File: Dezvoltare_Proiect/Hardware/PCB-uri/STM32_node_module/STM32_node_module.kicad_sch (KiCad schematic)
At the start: 4 parts, among them U1 STM32F411RETx, U2 ATECC608B-SSHDA, U3 SHT30A-DIS

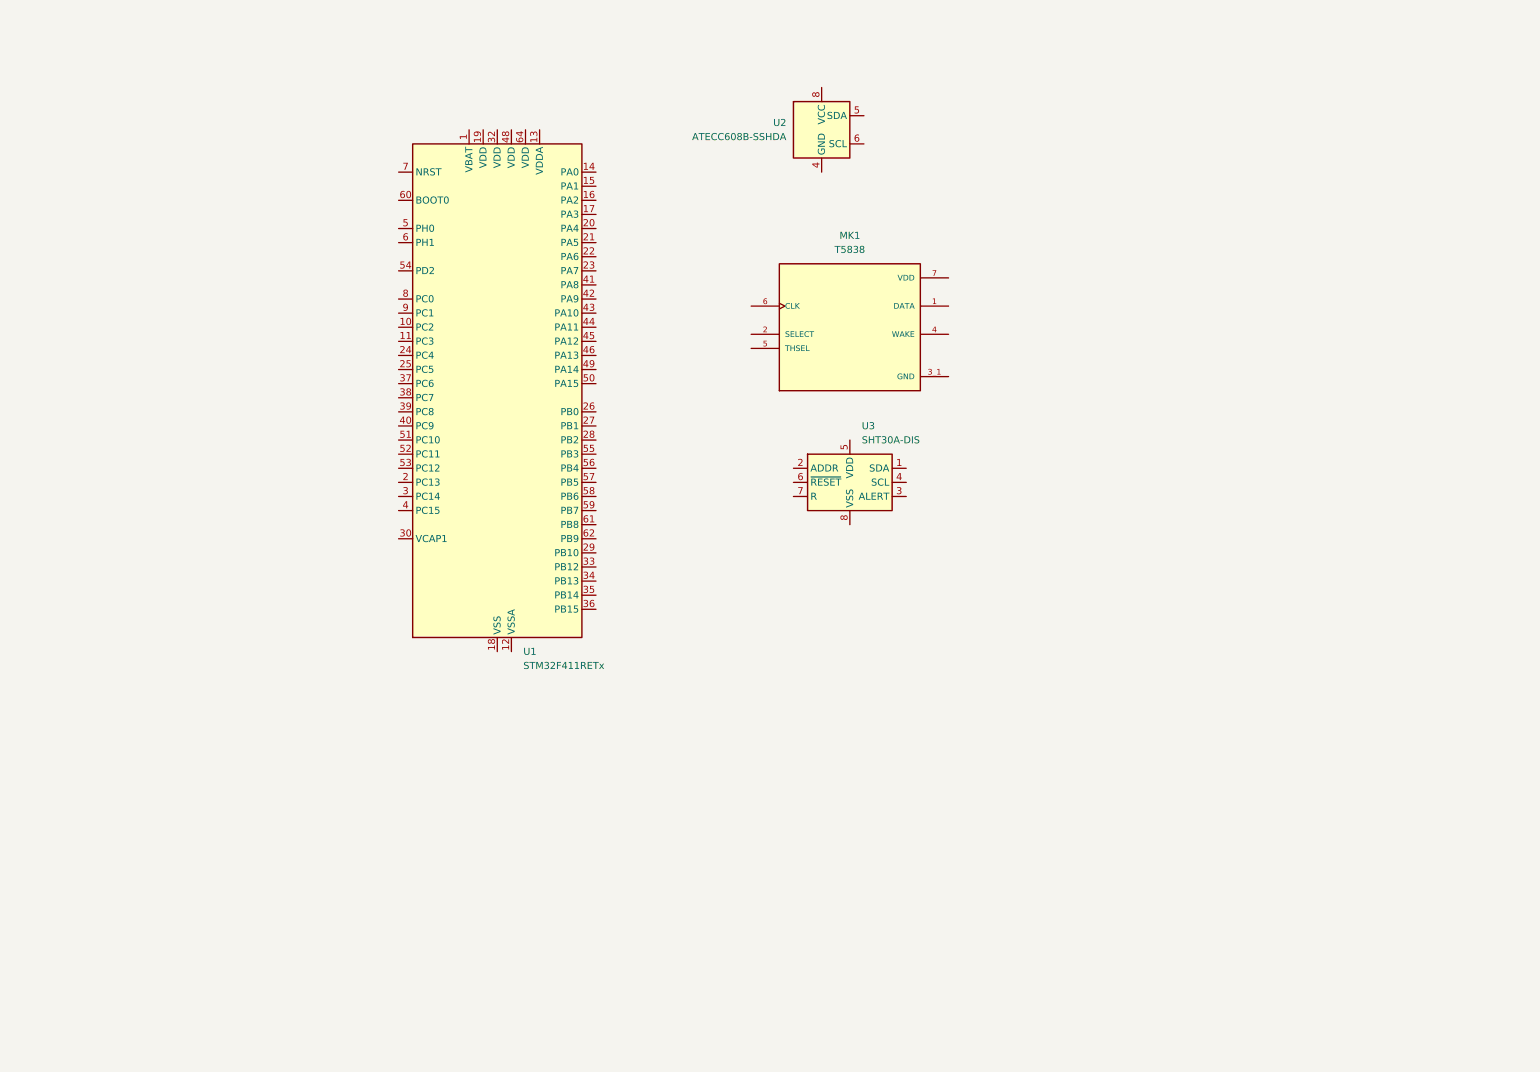
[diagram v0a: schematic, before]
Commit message: Actualizare PCB-uri, componente custom, acces la documentatia de pe overleaf.
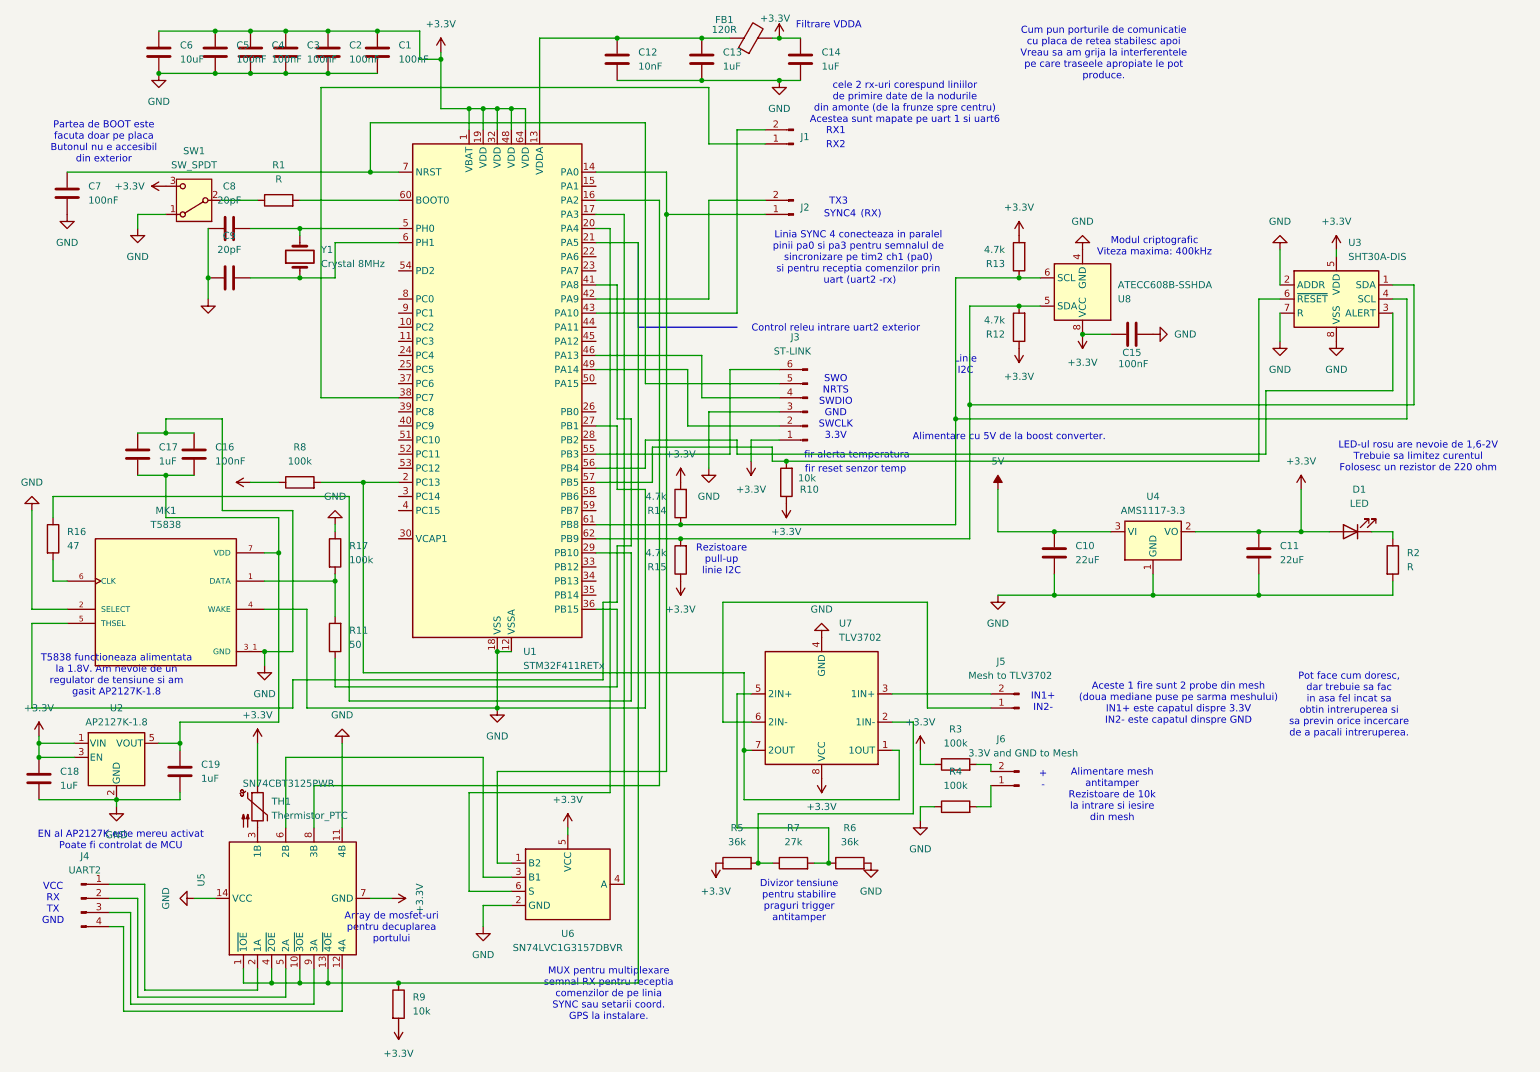
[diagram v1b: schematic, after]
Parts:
- removed U2: ATECC608B-SSHDA, Package_SO:SOIC-8_3.9x4.9mm_P1.27mm, symbol Security:ATECC608B-SSHDA
- added C1, C15, C16, C2, C3, C4, C5, C7: 100nF, symbol Device:C
- added C10, C11: 22uF, symbol Device:C
- added C12: 10nF, symbol Device:C
- added C13, C14, C17, C18, C19: 1uF, symbol Device:C
- added C6: 10uF, symbol Device:C
- added C8, C9: 20pF, symbol Device:C
- added D1: LED, symbol Device:LED
- added FB1: 120R, symbol Device:FerriteBead
- added J1, J2: (no value), symbol Connector:Conn_01x02_Pin
- added J3: ST-LINK, symbol Connector:Conn_01x06_Pin
- added J4: UART2, symbol Connector:Conn_01x04_Pin
- added J5: Mesh to TLV3702, symbol Connector:Conn_01x02_Pin
- added J6: 3.3V and GND to Mesh, symbol Connector:Conn_01x02_Pin
- added R1, R2: R, symbol Device:R
- added R10, R9: 10k, symbol Device:R
- added R11: 50, symbol Device:R
- added R12, R13, R14, R15: 4.7k, symbol Device:R
- added R16: 47, symbol Device:R
- added R17, R3, R4, R8: 100k, symbol Device:R
- added R5, R6: 36k, symbol Device:R
- added R7: 27k, symbol Device:R
- added SW1: SW_SPDT, symbol Switch:SW_SPDT
- added TH1: Thermistor_PTC, symbol Device:Thermistor_PTC
- added U2: AP2127K-1.8, Package_TO_SOT_SMD:SOT-23-5, symbol Regulator_Linear:AP2127K-1.8
- added U4: AMS1117-3.3, Package_TO_SOT_SMD:SOT-223-3_TabPin2, symbol Regulator_Linear:AMS1117-3.3
- added U5: SN74CBT3125PWR, Custom_Footprints:TSSOP-14_PW14_TI, symbol SN74CBT3125_PW:SN74CBT3125PWR
- added U6: SN74LVC1G3157DBVR, Custom_Footprints:SOT-23-6_DBV0006A, symbol SN74LVC1G3157_DBV:SN74LVC1G3157DBVR
- added U7: TLV3702, Custom_Footprints:SOIC-8_3.9x4.9mm_P1.27mm, symbol TLV3702:TLV3702
- added U8: ATECC608B-SSHDA, Package_SO:SOIC-8_3.9x4.9mm_P1.27mm, symbol Security:ATECC608B-SSHDA
- added Y1: Crystal 8MHz, symbol Device:Crystal
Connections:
- net GND: now also MK1.2 (SELECT), MK1.4 (WAKE), U1.12 (VSSA), U1.18 (VSS), U1.27 (PB1), U1.31 (VSS), U1.47 (VSS), U1.63 (VSS), U3.2 (ADDR), U3.7 (R), U3.8 (VSS), U3.9 (VSS), C1.2, C10.2, C11.2, C12.2, C13.2, C14.2, C15.2, C16.2, C17.1, C18.2, C19.2, C2.2, C3.2, C4.2, C5.2, C6.2, C7.2, C8.1, C9.1, J3.3 (Pin_3), R17.1, R2.2, R4.1, R6.2, SW1.1 (A), U2.2 (GND), U4.1 (GND), U5.11 (4B), U5.14 (VCC), U6.2 (GND), U7.4 (GND), U8.4 (GND)
- net +3.3V: now reaches U1.1 (VBAT)
- net +3.3V: now also U1.19 (VDD), U1.32 (VDD), U1.48 (VDD), U1.64 (VDD), U3.5 (VDD), C1.1, C11.1, C14.1, C15.1, C18.1, C2.1, C3.1, C4.1, C5.1, C6.1, D1.2 (A), FB1.2, J3.1 (Pin_1), R10.1, R12.1, R13.2, R14.2, R15.1, R3.1, R5.1, R8.1, R9.2, SW1.3 (C), TH1.1, U2.1 (VIN), U2.3 (EN), U4.2 (VO), U5.7 (GND), U6.5 (VCC), U7.8 (VCC), U8.8 (VCC)
- net at U1.13 (VDDA): now also C12.1, C13.1, FB1.1
- net at U1.14 (PA0): now also J2.1 (Pin_1), U6.1 (B2)
- net at U1.16 (PA2): now also U5.8 (3B)
- net at U1.17 (PA3): now also U6.4 (A)
- net at U1.2 (PC13): now also R8.2, U7.1 (1OUT), U7.7 (2OUT)
- net at U1.20 (PA4): now also U6.6 (S)
- net at U1.21 (PA5): now also R9.1, U5.1 (~{1OE}), U5.10 (~{3OE}), U5.13 (~{4OE}), U5.4 (~{2OE})
- net at U1.29 (PB10): now also R16.1
- net at U1.36 (PB15): now also R11.1
- net at U1.38 (PC7): now also J1.1 (Pin_1)
- net at U1.41 (PA8): now also MK1.5 (THSEL)
- net at U1.42 (PA9): now also J2.2 (Pin_2)
- net at U1.43 (PA10): now also J1.2 (Pin_2)
- net at U1.46 (PA13): now also J3.4 (Pin_4)
- net at U1.49 (PA14): now also J3.2 (Pin_2)
- net at U1.5 (PH0): now also C8.2, Y1.2
- net at U1.55 (PB3): now also J3.6 (Pin_6)
- net at U1.56 (PB4): now also U3.3 (ALERT)
- net at U1.57 (PB5): now also U3.6 (~{RESET}), R10.2
- net at U1.6 (PH1): now also C9.2, Y1.1
- net at U1.60 (BOOT0): now also R1.2
- net at U1.61 (PB8): now also U3.4 (SCL), R13.1, R14.1, U8.6 (SCL)
- net at U1.62 (PB9): now also U3.1 (SDA), R12.2, R15.2, U8.5 (SDA)
- net at U1.7 (NRST): now also C7.1, J3.5 (Pin_5)
- net at MK1.1 (DATA): now also R11.2, R17.2
- net at MK1.6 (CLK): now also R16.2
- net at MK1.7 (VDD): now also C16.1, C17.2, C19.1, U2.5 (VOUT)
- new net: J4.4 (Pin_4), U5.12 (4A)
- new net: J4.1 (Pin_1), U5.2 (1A)
- new net: TH1.2, U5.3 (1B)
- new net: J4.2 (Pin_2), U5.5 (2A)
- new net: U5.6 (2B), U6.3 (B1)
- new net: J4.3 (Pin_3), U5.9 (3A)
- new net: R5.2, R7.1, U7.2 (1IN-)
- new net: R6.1, R7.2, U7.5 (2IN+)
- new net: J6.1 (Pin_1), R4.2
- new net: J6.2 (Pin_2), R3.2
- new net: J5.1 (Pin_1), U7.6 (2IN-)
- new net: J5.2 (Pin_2), U7.3 (1IN+)
- new net: R1.1, SW1.2 (B)
- new net: D1.1 (K), R2.1
- new net 5V: C10.1, U4.3 (VI)
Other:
- note added: "(RX)"
- note added: "+ -"
- note added: "Aceste 1 fire sunt 2 probe din mesh (doua mediane puse pe sarma meshului) IN1+ este capatul dispre 3.3V IN2- este capatul dinspre GND"
- note added: "Alimentare cu 5V de la boost converter."
- note added: "Alimentare mesh antitamper Rezistoare de 10k la intrare si iesire din mesh"
- note added: "Array de mosfet-uri pentru decuplarea portului"
- note added: "Control releu intrare uart2 exterior"
- note added: "Cum pun porturile de comunicatie cu placa de retea stabilesc apoi Vreau sa am grija la interferentele pe care traseele apropiate le pot produce."
- note added: "Divizor tensiune pentru stabilire praguri trigger antitamper"
- note added: "EN al AP2127K este mereu activat Poate fi controlat de MCU"
- note added: "Filtrare VDDA"
- note added: "IN1+ IN2-"
- note added: "LED-ul rosu are nevoie de 1,6-2V Trebuie sa limitez curentul Folosesc un rezistor de 220 ohm"
- note added: "Linia SYNC 4 conecteaza in paralel pinii pa0 si pa3 pentru semnalul de sincronizare pe tim2 ch1 (pa0) si pentru receptia comenzilor prin uart (uart2 -rx)"
- note added: "Linie I2C"
- note added: "MUX pentru multiplexare semnal RX pentru receptia comenzilor de pe linia SYNC sau setarii coord. GPS la instalare."
- note added: "Modul criptografic Viteza maxima: 400kHz"
- note added: "Partea de BOOT este facuta doar pe placa Butonul nu e accesibil din exterior"
- note added: "Pot face cum doresc, dar trebuie sa fac in asa fel incat sa obtin intreruperea si sa previn orice incercare de a pacali intreruperea."
- note added: "RX1"
- note added: "RX2"
- note added: "Rezistoare pull-up linie I2C"
- note added: "SWO NRTS SWDIO GND SWCLK 3.3V"
- note added: "SYNC4"
- note added: "T5838 functioneaza alimentata la 1.8V. Am nevoie de un regulator de tensiune si am gasit AP2127K-1.8"
- note added: "TX3"
- note added: "VCC RX TX GND"
- note added: "cele 2 rx-uri corespund liniilor de primire date de la nodurile din amonte (de la frunze spre centru) Acestea sunt mapate pe uart 1 si uart6"
- note added: "fir alerta temperatura"
- note added: "fir reset senzor temp"
- moved on the sheet: MK1, U3

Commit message: Primul driver pentru T5838. Am citit datasheetul bine si am configurat secventa de initializare pentru a putea utiliza modul de operare AAD D2 al microfonului, apoi am configurat frecventa astfel incat microfonul sa poata receptiona sunetele din mediu (pentru moment, sunetele din camera). Maine am sa continui sa ma joc cu acest microfon si sa explorez manual capabilitatile sale. Tot maine am sa scriu de mana driverul pentru secventa de initializare si accesare a modului AAD D2 conform datasheetului. Am vazut ca acest microfon funcitoneaza in stransa legatura cu frecventa CLK. AAD D2 permit trimiterea unei intreruperi cand sunetul depaseste anumite praguri de decibeli si de durata, cu CLK pe OFF. Apoi MCU se trezeste, bate frecventa de ceas la 2MHz pentru detalii acustice bune, iar sunetul este receptionat in format PDM. Pe STM trebuie facuta conversia la PCM, apoi efectuate alte operatii.
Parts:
- removed R13: 4.7k, symbol Device:R
- added C20: 2.2uF, Capacitor_SMD:C_0805_2012Metric, symbol Device:C
- added D2: VERDE - Retea status, symbol Device:LED
- added D3: ROSU - GPS status, symbol Device:LED
- added D4: GABLEN - external UART port, symbol Device:LED
- added R18: 330, Resistor_SMD:R_0805_2012Metric, symbol Device:R
- added R19, R20: 1k, Resistor_SMD:R_0805_2012Metric, symbol Device:R
- added SW2: Manual_RST, symbol Switch:SW_Push
- C1, C10, C11, C12, C13, C14, C15, C16, C17, C18, C19, C2, C3, C4, C5, C6, C7: footprint (none) -> Capacitor_SMD:C_0805_2012Metric
- R1: value R -> 100k; footprint (none) -> Resistor_SMD:R_0805_2012Metric
- R10, R11, R14, R15, R16, R17, R3, R4, R5, R6, R7, R8, R9: footprint (none) -> Resistor_SMD:R_0805_2012Metric
- R12: value 4.7k -> 10k; footprint (none) -> Resistor_SMD:R_0805_2012Metric
- R2: value R -> 1k; footprint (none) -> Resistor_SMD:R_0805_2012Metric
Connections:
- net +3.3V: now also U5.14 (VCC); no longer R12.1, U5.7 (GND)
- net GND: now also R12.1, U5.7 (GND), C20.2, R18.2, R19.2, R20.2, SW2.2; no longer MK1.4 (WAKE), U1.27 (PB1), U5.14 (VCC)
- net SDA_line: now reaches R15.2, U1.62 (PB9), U3.1 (SDA), U8.5 (SDA)
- net SDA_line: no longer R12.2
- net GATE_UART2_control: now reaches R9.1, U1.21 (PA5), U5.1 (~{1OE}), U5.10 (~{3OE}), U5.13 (~{4OE}), U5.4 (~{2OE})
- net at U5.6 (2B): now also U6.1 (B2); no longer U6.3 (B1)
- net TX_UART2: now reaches U1.16 (PA2), U5.8 (3B)
- net TAMPER_INTERRUPT: now reaches R8.2, U1.2 (PC13), U7.1 (1OUT), U7.7 (2OUT)
- net SCL_line: now reaches R14.1, U1.61 (PB8), U3.4 (SCL), U8.6 (SCL)
- net SYNC_LINE: now reaches J2.1 (Pin_1), U1.14 (PA0)
- net SYNC_LINE: now also U6.3 (B1); no longer U6.1 (B2)
- net RX_UART2: now reaches U1.17 (PA3), U6.4 (A)
- net MUX_SELECT: now reaches U1.20 (PA4), U6.6 (S)
- net MUX_SELECT: now also R12.2
- net !RESET: now reaches R10.2, U1.57 (PB5), U3.6 (~{RESET})
- net CLK: now reaches R16.1, U1.29 (PB10)
- net at U1.30 (VCAP1): now also C20.1
- net network_status: now reaches U1.33 (PB12)
- net network_status: now also D2.2 (A)
- net UART2_status: now reaches U1.34 (PB13)
- net UART2_status: now also D4.2 (A)
- net GPS_status: now reaches U1.35 (PB14)
- net GPS_status: now also D3.2 (A)
- net DATA: now reaches R11.1, U1.36 (PB15)
- net THSEL: now reaches MK1.5 (THSEL), U1.41 (PA8)
- net ALERT: now reaches U1.56 (PB4), U3.3 (ALERT)
- net at C7.1, J3.5 (Pin_5), U1.7 (NRST): now also SW2.1
- new net: D3.1 (K), R19.1
- new net: D4.1 (K), R20.1
- new net: D2.1 (K), R18.1
- new net WAKE: MK1.4 (WAKE), U1.27 (PB1)
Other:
- note added: "MUX-ul va permite by default semnalului SYNC sa treaca (S=LOW). La activare, se chimba canalul pe intrarea GPS (S=HIGH)"
- note added: "Pull down pentru MUX select pin"
- note added: "Sync & interrupt"
- note added: "UART2 RX"
- note added: "UART2 TX"
- note removed: "Rezistoare pull-up linie I2C"
- moved on the sheet: C1, J3, R10, R14, R15
